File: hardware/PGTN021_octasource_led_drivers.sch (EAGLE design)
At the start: 130 parts, among them IC1 TL084P, IC2 TL084P, IC3 TL084P, IC4 TL084P

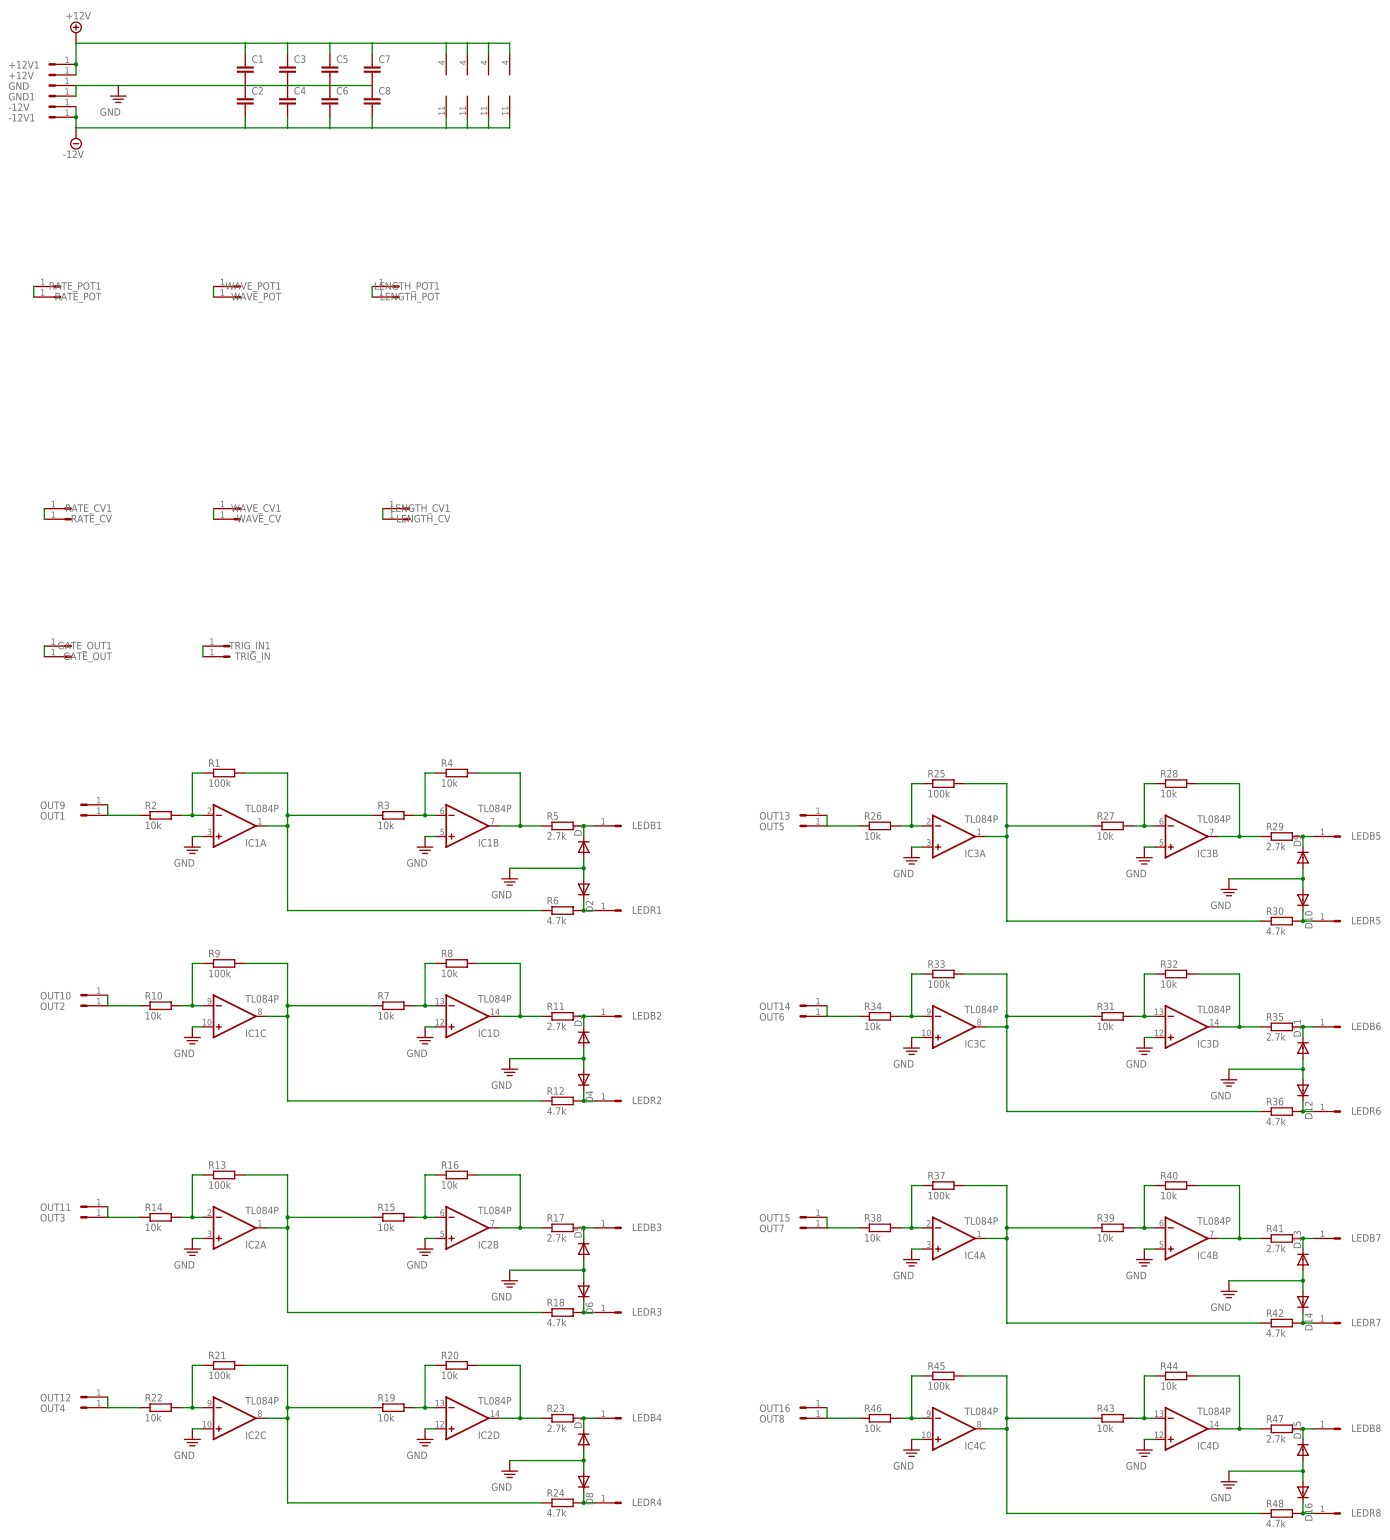
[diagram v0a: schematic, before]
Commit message: added capacitor values
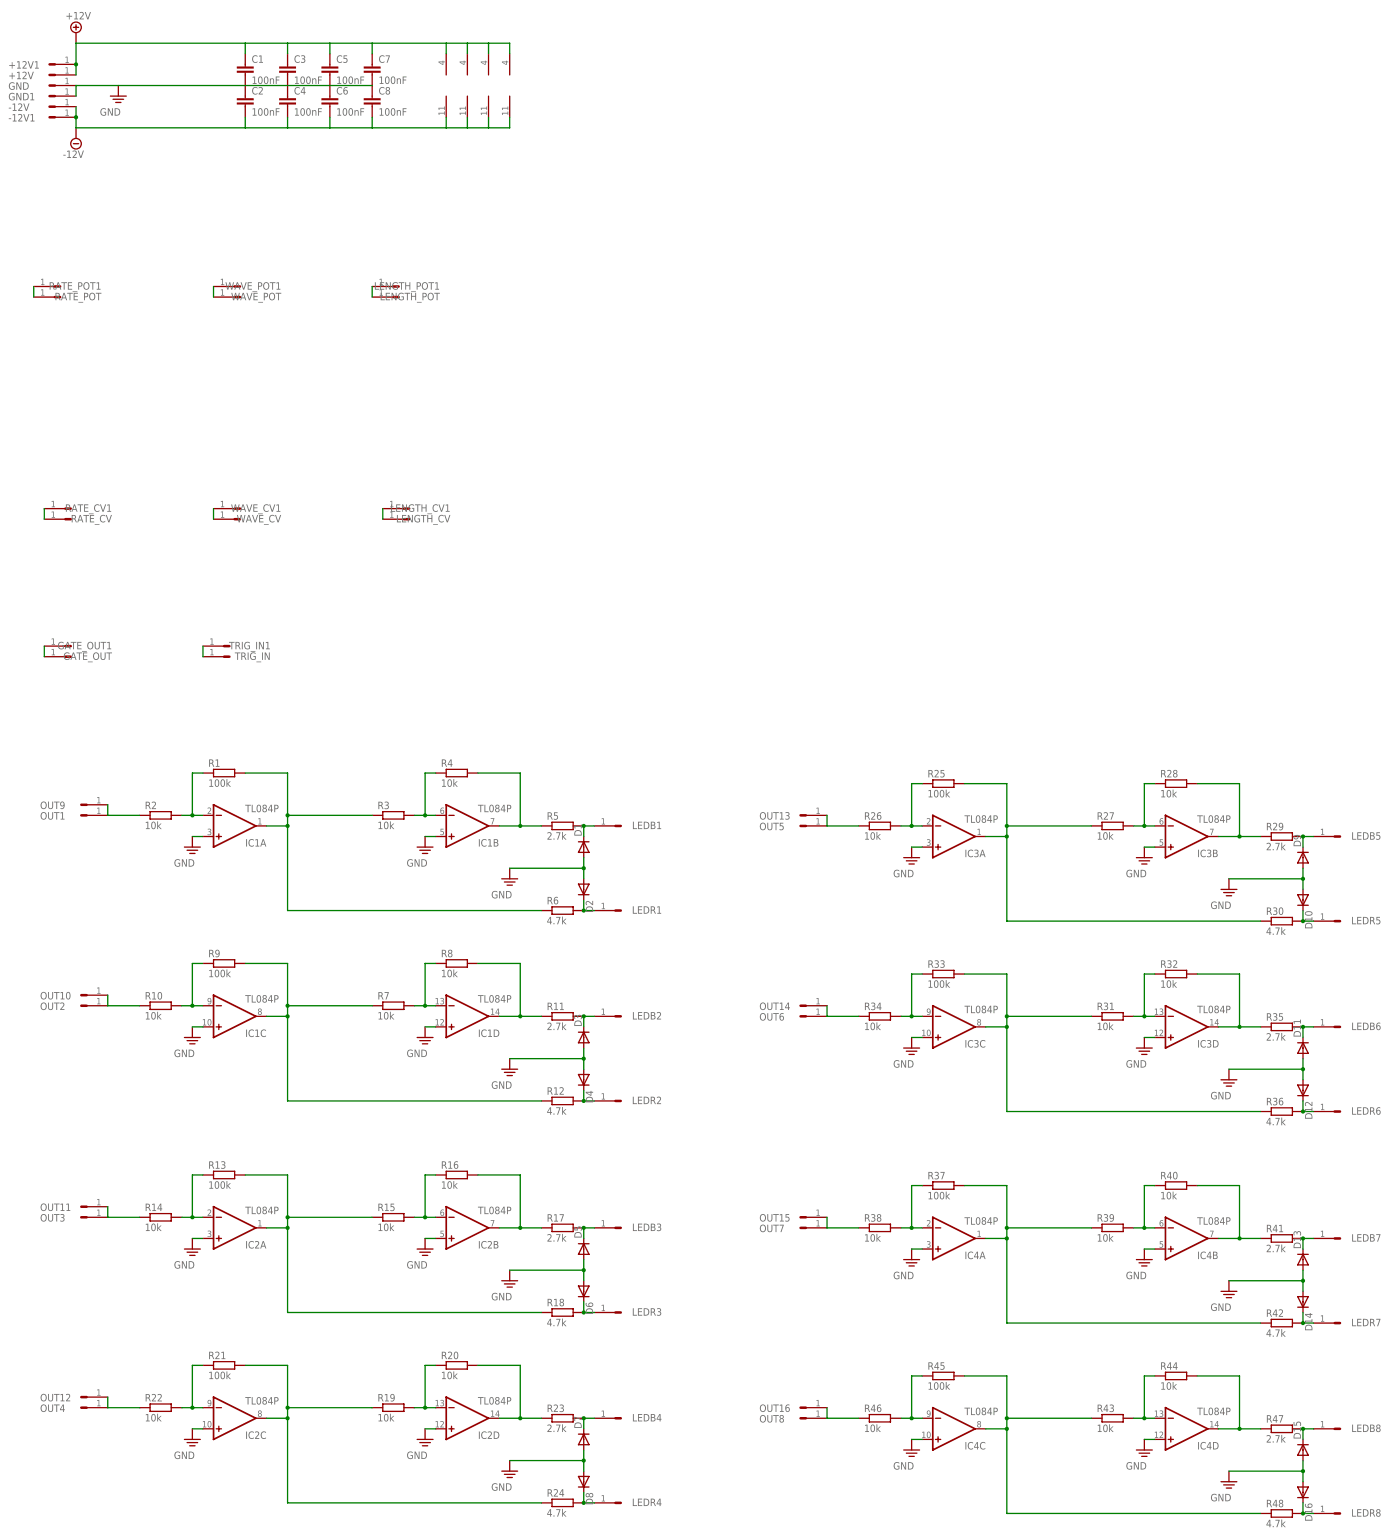
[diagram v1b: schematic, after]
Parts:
- C1, C2, C3, C4, C5, C6, C7, C8: value (none) -> 100nF
